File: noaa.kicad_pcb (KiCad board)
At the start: 2 copper layers, 28.5 x 20 mm, 15 parts, among them J1 USB_C_Receptacle_USB2.0_16P, J2 SMA_F_INT, J3 SMA_F_OUT, U3 GALI-84

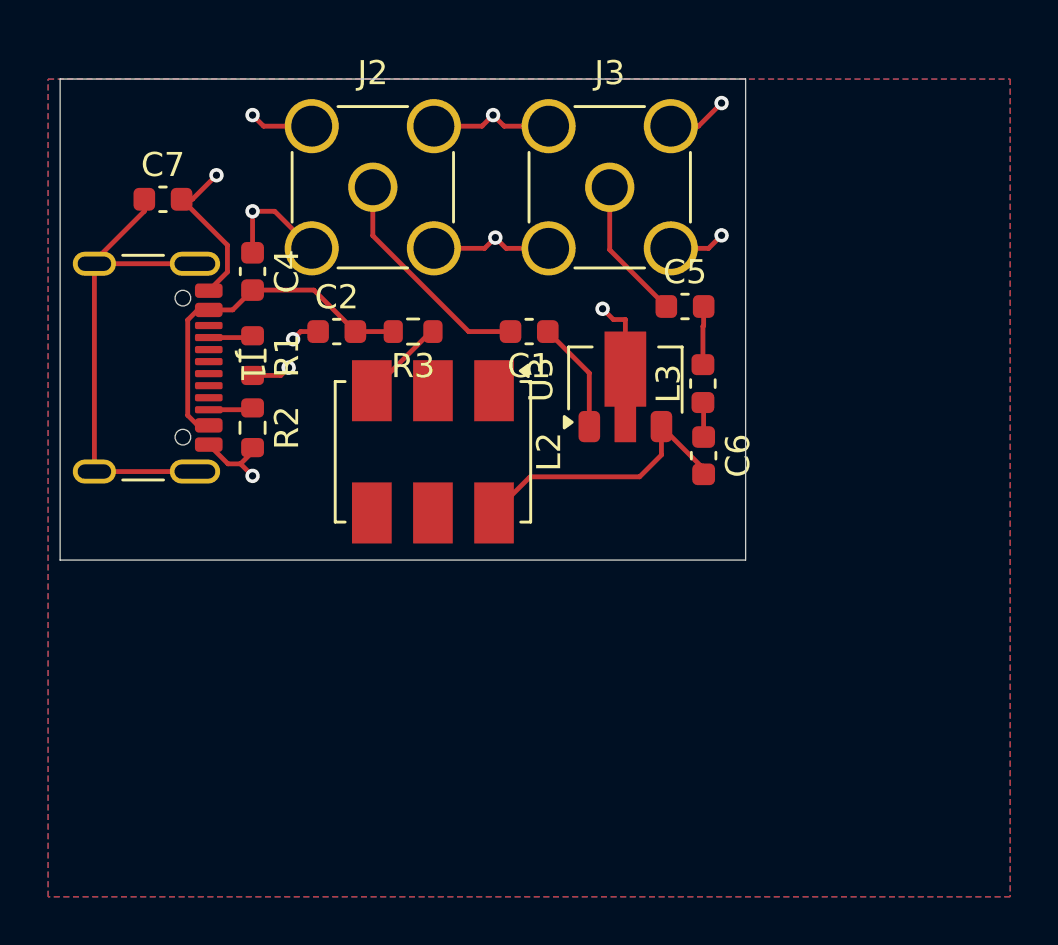
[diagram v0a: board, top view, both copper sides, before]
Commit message: Did some ground stitching and added prod files
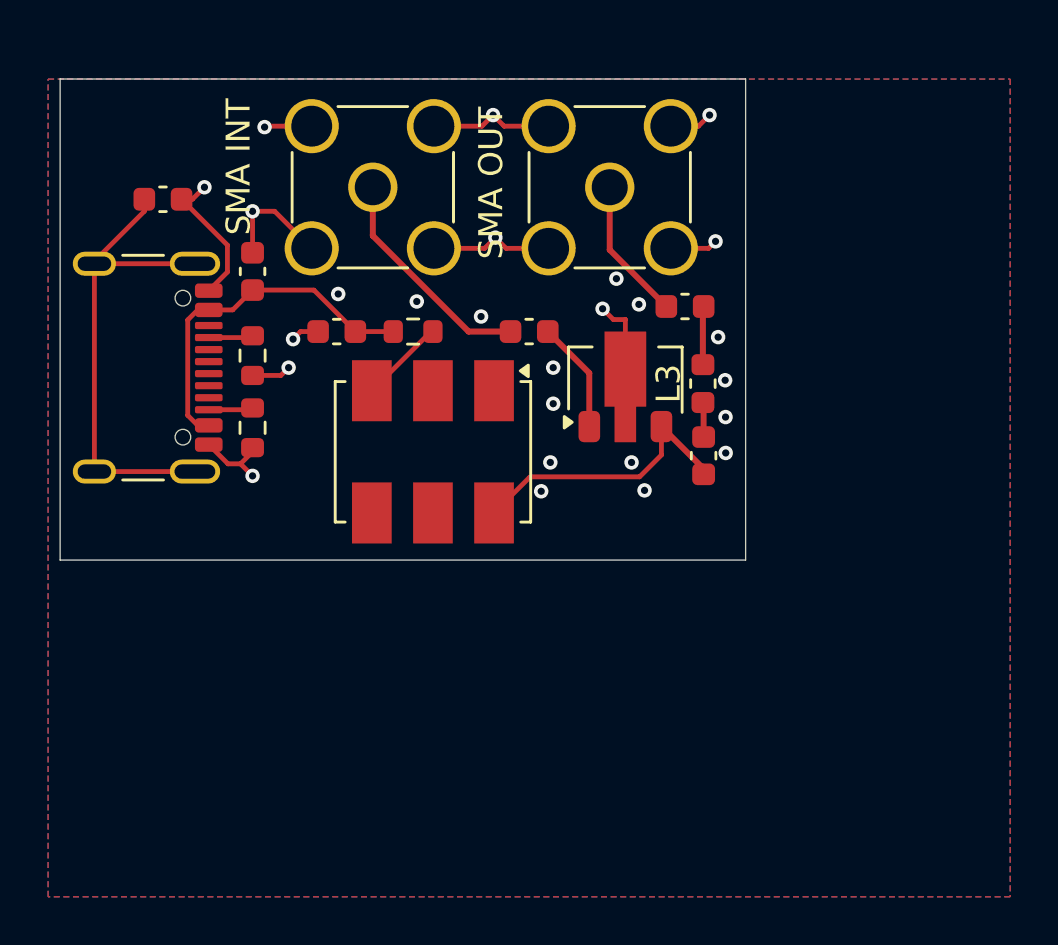
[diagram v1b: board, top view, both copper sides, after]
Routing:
- net GND: track 40.9 -> 38.5 mm, vias 11 -> 26
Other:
- board text added: "SMA INT"
- board text added: "SMA OUT"

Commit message: Mounting holes x3 + STEP File
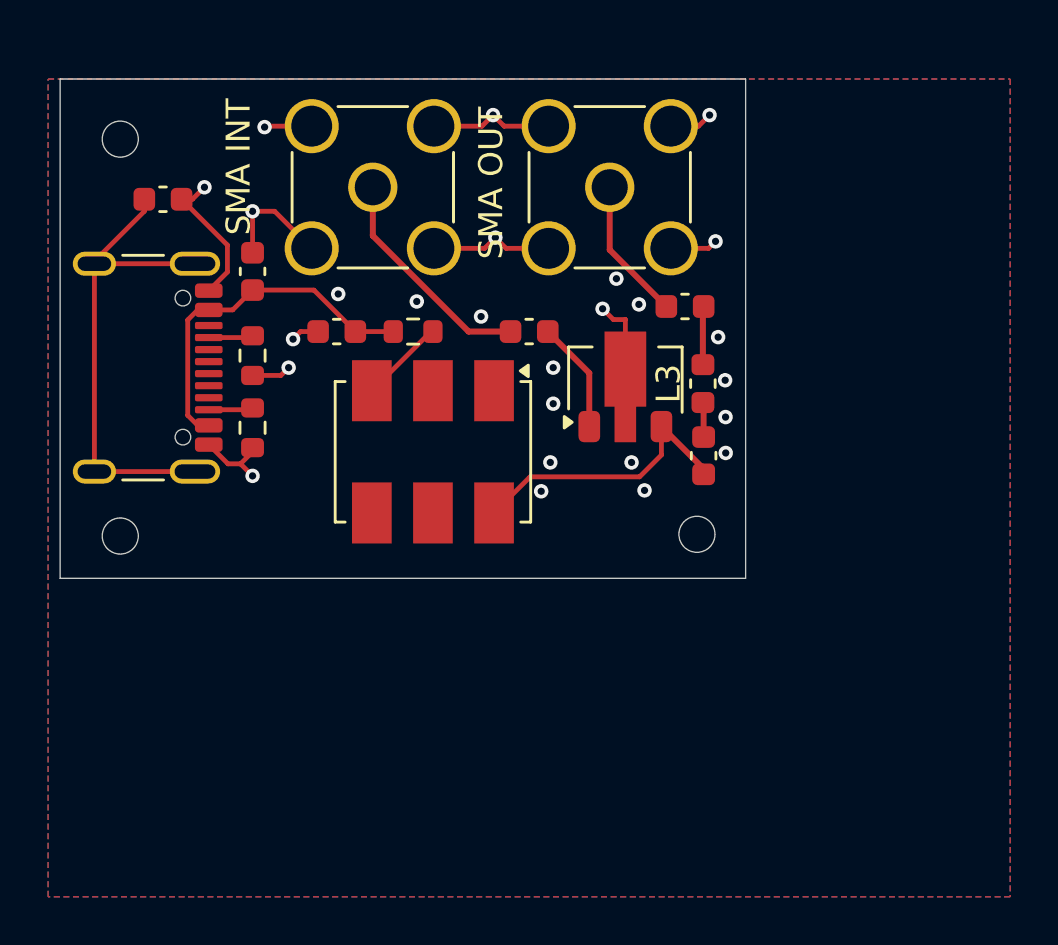
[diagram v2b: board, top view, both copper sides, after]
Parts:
- added REF**: MountingHole_2.1mm, MountingHole:MountingHole_2.1mm, F.Cu at (103.0, 75.5)
- added REF**: MountingHole_2.1mm, MountingHole:MountingHole_2.1mm, F.Cu at (127.0, 75.4)
- added REF**: MountingHole_2.1mm, MountingHole:MountingHole_2.1mm, F.Cu at (103.0, 59.0)
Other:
- board size 28.5 x 20 mm -> 28.5 x 20.8 mm

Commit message: Added my case that took a full day to make :(
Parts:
- removed the REF** at (127.0, 75.4)
- removed the REF** at (103.0, 59.0)
- added ?: , , F.Cu at (126.5, 75.5)
- added ?: , , F.Cu at (102.5, 58.5)
- REF**: moved to B.Cu
- turned REF** to 180 degrees
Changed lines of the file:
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@@
 	(net 21 "Net-(L2-DC)")
 	(net 22 "unconnected-(L2-NC-Pad5)")
-	(footprint "MountingHole:MountingHole_2.1mm"
+	(footprint ""
 		(layer "F.Cu")
-		(at 103 75.5)
-		(descr "Mounting Hole 2.1mm, no annular, generated by kicad-footprint-generator mountinghole.py")
-		(tags "mountinghole")
-		(property "Reference" "REF**"
-			(at 0 -3.05 0)
+		(at 126.5 75.5)
+		(property "Reference" ""
+			(at 0 0 0)
 			(layer "F.SilkS")
-			(hide yes)
 			(effects
 				(font
-					(size 1 1)
+					(size 1.27 1.27)
 					(thickness 0.15)
 				)
 			)
 		)
-		(property "Value" "MountingHole_2.1mm"
-			(at 0 3.05 0)
+		(property "Value" ""
+			(at 0 0 0)
 			(layer "F.Fab")
-			(hide yes)
 			(effects
 				(font
-					(size 1 1)
+					(size 1.27 1.27)
 					(thickness 0.15)
 				)
@@
 			)
 		)
-		(attr exclude_from_pos_files exclude_from_bom)
-		(fp_circle
-			(center 0 0)
-			(end 1.276619 0.073986)
-			(stroke
-				(width 0.15)
-				(type solid)
-			)
-			(fill no)
-			(layer "Cmts.User")
-		)
-		(fp_circle
-			(center 0 0)
-			(end 1.5 0)
-			(stroke
-				(width 0.05)
-				(type solid)
-			)
-			(fill no)
-			(layer "F.CrtYd")
-		)
 		(pad "" np_thru_hole circle
-			(at 0 0)
+			(at 0 0 180)
 			(size 0.670506 0.670506)
 			(drill 1.5)
@@
 		)
 	)
-	(footprint "MountingHole:MountingHole_2.1mm"
+	(footprint ""
 		(layer "F.Cu")
-		(at 126.976558 75.428683)
-		(descr "Mounting Hole 2.1mm, no annular, generated by kicad-footprint-generator mountinghole.py")
-		(tags "mountinghole")
-		(property "Reference" "REF**"
-			(at 0 -3.05 0)
+		(at 102.5 58.5)
+		(property "Reference" ""
+			(at 0 0 0)
 			(layer "F.SilkS")
-			(hide yes)
 			(effects
 				(font
-					(size 1 1)
+					(size 1.27 1.27)
 					(thickness 0.15)
 				)
 			)
 		)
-		(property "Value" "MountingHole_2.1mm"
-			(at 0 3.05 0)
+		(property "Value" ""
+			(at 0 0 0)
 			(layer "F.Fab")
-			(hide yes)
 			(effects
 				(font
-					(size 1 1)
+					(size 1.27 1.27)
 					(thickness 0.15)
 				)
@@
 			)
 		)
-		(attr exclude_from_pos_files exclude_from_bom)
-		(fp_circle
-			(center 0 0)
-			(end 1.276619 0.073986)
-			(stroke
-				(width 0.15)
-				(type solid)
-			)
-			(fill no)
-			(layer "Cmts.User")
-		)
-		(fp_circle
-			(center 0 0)
-			(end 1.5 0)
-			(stroke
-				(width 0.05)
-				(type solid)
-			)
-			(fill no)
-			(layer "F.CrtYd")
-		)
 		(pad "" np_thru_hole circle
-			(at 0 0)
+			(at 0 0 180)
 			(size 0.670506 0.670506)
 			(drill 1.5)
@@
 		)
 	)
-	(footprint "MountingHole:MountingHole_2.1mm"
-		(layer "F.Cu")
-		(at 103 59)
-		(descr "Mounting Hole 2.1mm, no annular, generated by kicad-footprint-generator mountinghole.py")
-		(tags "mountinghole")
-		(property "Reference" "REF**"
-			(at 0 -3.05 0)
-			(layer "F.SilkS")
-			(hide yes)
-			(effects
-				(font
-					(size 1 1)
-					(thickness 0.15)
-				)
-			)
-		)
-		(property "Value" "MountingHole_2.1mm"
-			(at 0 3.05 0)
-			(layer "F.Fab")
-			(hide yes)
-			(effects
-				(font
-					(size 1 1)
-					(thickness 0.15)
-				)
-			)
-		)
-		(property "Datasheet" ""
-			(at 0 0 0)
-			(layer "F.Fab")
-			(hide yes)
-			(effects
-				(font
-					(size 1.27 1.27)
-					(thickness 0.15)
-				)
-			)
-		)
-		(property "Description" ""
-			(at 0 0 0)
-			(layer "F.Fab")
-			(hide yes)
-			(effects
-				(font
-					(size 1.27 1.27)
-					(thickness 0.15)
-				)
-			)
-		)
-		(attr exclude_from_pos_files exclude_from_bom)
-		(fp_circle
-			(center 0 0)
-			(end 1.276619 0.073986)
-			(stroke
-				(width 0.15)
-				(type solid)
-			)
-			(fill no)
-			(layer "Cmts.User")
-		)
-		(fp_circle
-			(center 0 0)
-			(end 1.5 0)
-			(stroke
-				(width 0.05)
-				(type solid)
-			)
-			(fill no)
-			(layer "F.CrtYd")
-		)
-		(pad "" np_thru_hole circle
-			(at 0 0)
-			(size 0.670506 0.670506)
-			(drill 1.5)
-			(layers "*.Cu" "*.Mask")
-		)
-		(embedded_fonts no)
-	)
 	(footprint "Capacitor_SMD:C_0603_1608Metric"
 		(layer "F.Cu")
@@
 		)
 	)
+	(footprint "MountingHole:MountingHole_2.1mm"
+		(layer "B.Cu")
+		(at 103 75.5 180)
+		(descr "Mounting Hole 2.1mm, no annular, generated by kicad-footprint-generator mountinghole.py")
+		(tags "mountinghole")
+		(property "Reference" "REF**"
+			(at 0 3.05 0)
+			(layer "B.SilkS")
+			(hide yes)
+			(effects
+				(font
+					(size 1 1)
+					(thickness 0.15)
+				)
+				(justify mirror)
+			)
+		)
+		(property "Value" "MountingHole_2.1mm"
+			(at 0 -3.05 0)
+			(layer "B.Fab")
+			(hide yes)
+			(effects
+				(font
+					(size 1 1)
+					(thickness 0.15)
+				)
+				(justify mirror)
+			)
+		)
+		(property "Datasheet" ""
+			(at 0 0 0)
+			(layer "B.Fab")
+			(hide yes)
+			(effects
+				(font
+					(size 1.27 1.27)
+					(thickness 0.15)
+				)
+				(justify mirror)
+			)
+		)
+		(property "Description" ""
+			(at 0 0 0)
+			(layer "B.Fab")
+			(hide yes)
+			(effects
+				(font
+					(size 1.27 1.27)
+					(thickness 0.15)
+				)
+				(justify mirror)
+			)
+		)
+		(attr exclude_from_pos_files exclude_from_bom)
+		(pad "" np_thru_hole circle
+			(at 0 0 180)
+			(size 0.670506 0.670506)
+			(drill 1.5)
+			(layers "*.Cu" "*.Mask")
+		)
+		(embedded_fonts no)
+	)
 	(gr_rect
